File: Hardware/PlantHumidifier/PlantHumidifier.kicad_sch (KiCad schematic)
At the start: 12 parts

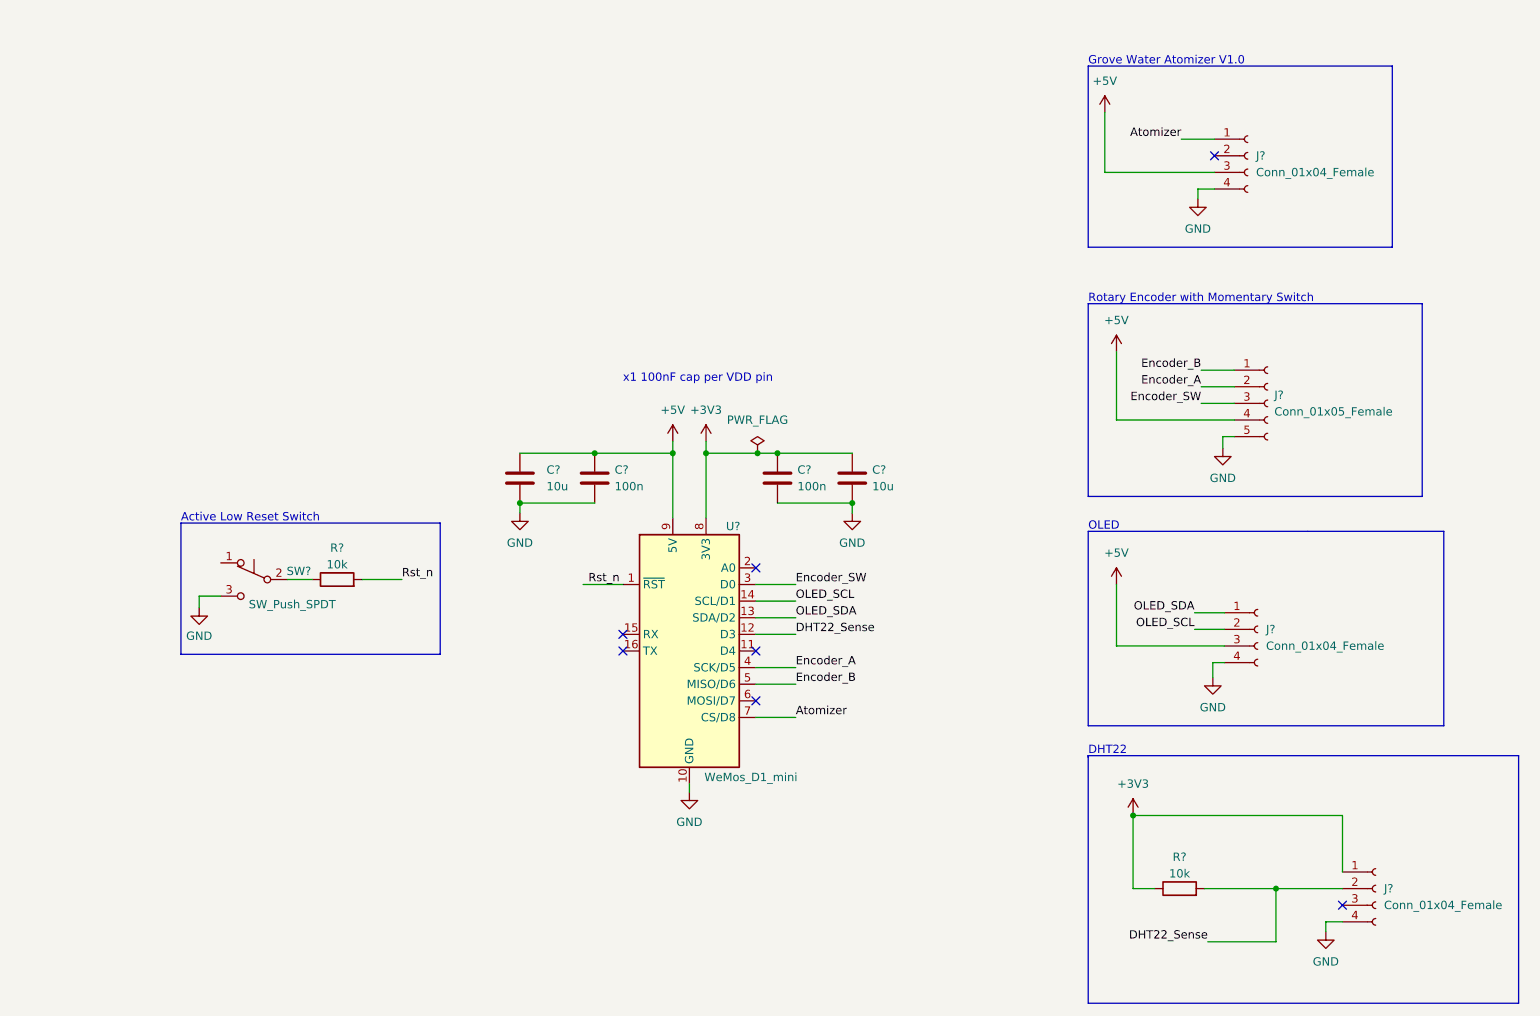
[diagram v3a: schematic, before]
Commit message: Schematic: Finish adding title and drawing outlines for different modules
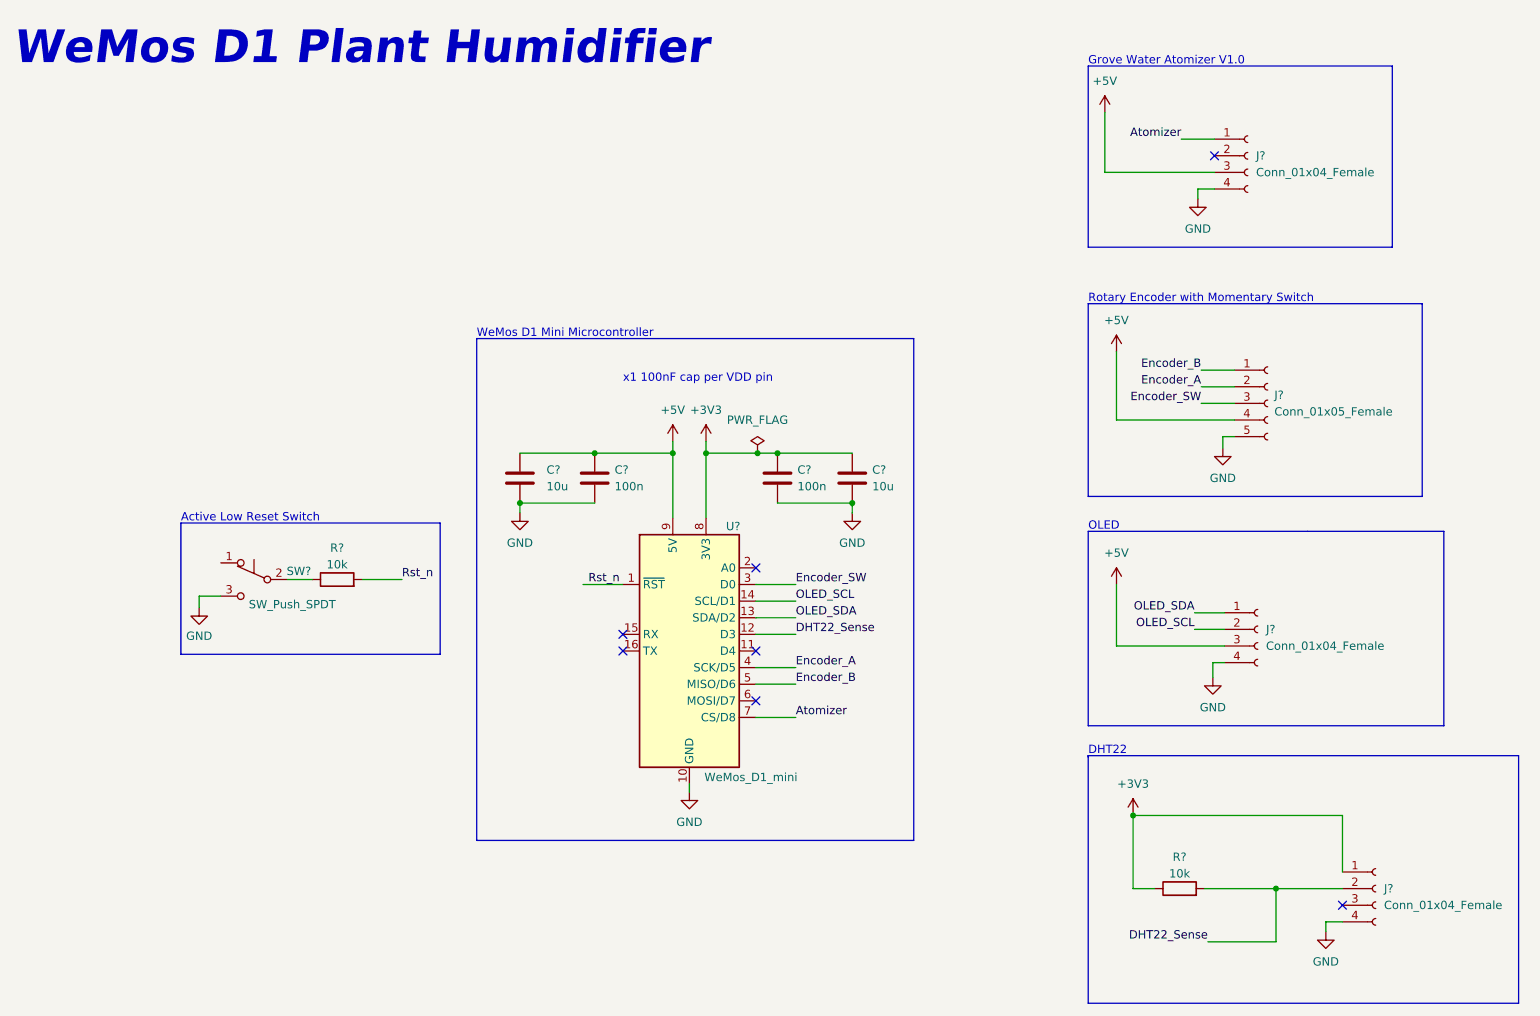
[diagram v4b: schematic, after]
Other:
- note added: "WeMos D1 Mini Microcontroller"
- note added: "WeMos D1 Plant Humidifier"
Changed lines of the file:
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@@
+    (stroke (width 0) (type default) (color 0 0 0 0))
+  )
+  (polyline (pts (xy 149.606 60.706) (xy 149.606 137.414))
     (stroke (width 0) (type default) (color 0 0 0 0))
   )
@@
     (stroke (width 0) (type default) (color 0 0 0 0))
   )
+  (polyline (pts (xy 82.804 137.414) (xy 82.804 60.706))
+    (stroke (width 0) (type default) (color 0 0 0 0))
+  )
   (wire (pts (xy 117.856 76.454) (xy 117.856 78.232))
     (stroke (width 0) (type default) (color 0 0 0 0))
@@
     (stroke (width 0) (type default) (color 0 0 0 0))
   )
+  (polyline (pts (xy 149.606 137.414) (xy 82.804 137.414))
+    (stroke (width 0) (type default) (color 0 0 0 0))
+  )
   (wire (pts (xy 178.816 26.162) (xy 178.816 35.306))
     (stroke (width 0) (type default) (color 0 0 0 0))
@@
     (stroke (width 0) (type default) (color 0 0 0 0))
   )
+  (polyline (pts (xy 82.804 60.706) (xy 149.606 60.706))
+    (stroke (width 0) (type default) (color 0 0 0 0))
+  )
   (polyline (pts (xy 37.592 108.966) (xy 37.592 88.9))
     (stroke (width 0) (type default) (color 0 0 0 0))
@@
     (effects (font (size 1.27 1.27)) (justify left bottom))
   )
+  (text "WeMos D1 Mini Microcontroller" (at 82.804 60.706 0)
+    (effects (font (size 1.27 1.27)) (justify left bottom))
+  )
   (text "Active Low Reset Switch" (at 37.592 88.9 0)
     (effects (font (size 1.27 1.27)) (justify left bottom))
   )
+  (text "WeMos D1 Plant Humidifier" (at 11.938 19.304 0)
+    (effects (font (size 5 5) (thickness 0.508) bold italic) (justify left bottom))
+  )
   (label "OLED_SDA" (at 131.572 103.378 0)

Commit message: Schematic: Annotate schematic
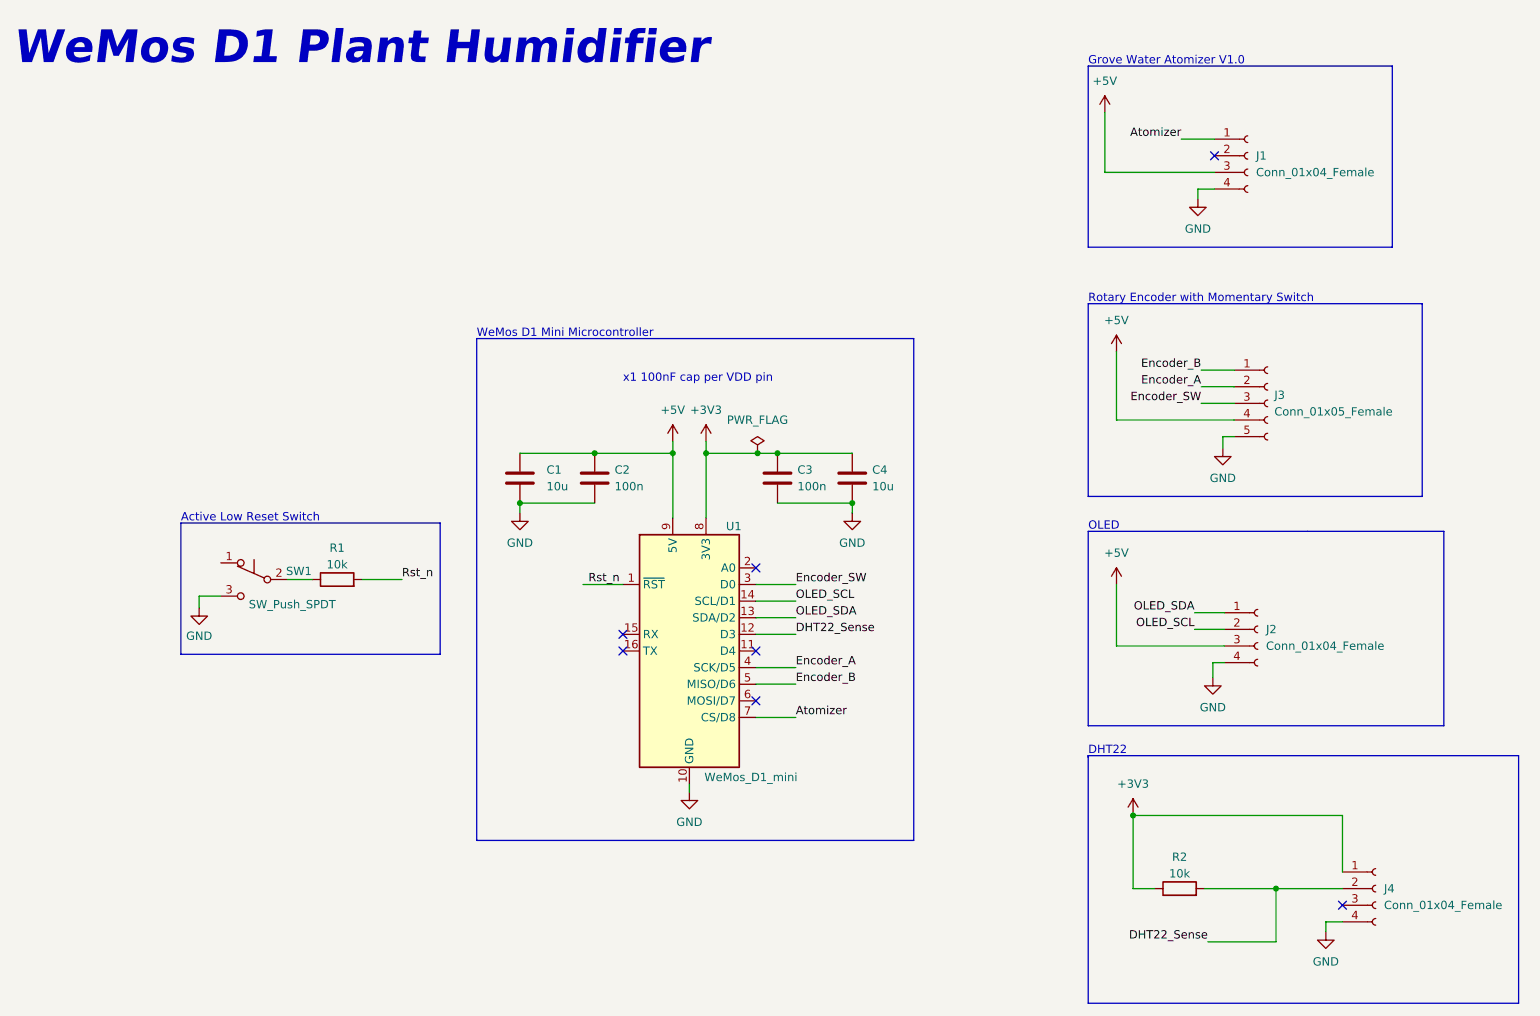
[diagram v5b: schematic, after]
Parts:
- gave numbers to parts that had none: 12

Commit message: Schematic: Run and fix DRC + Add power
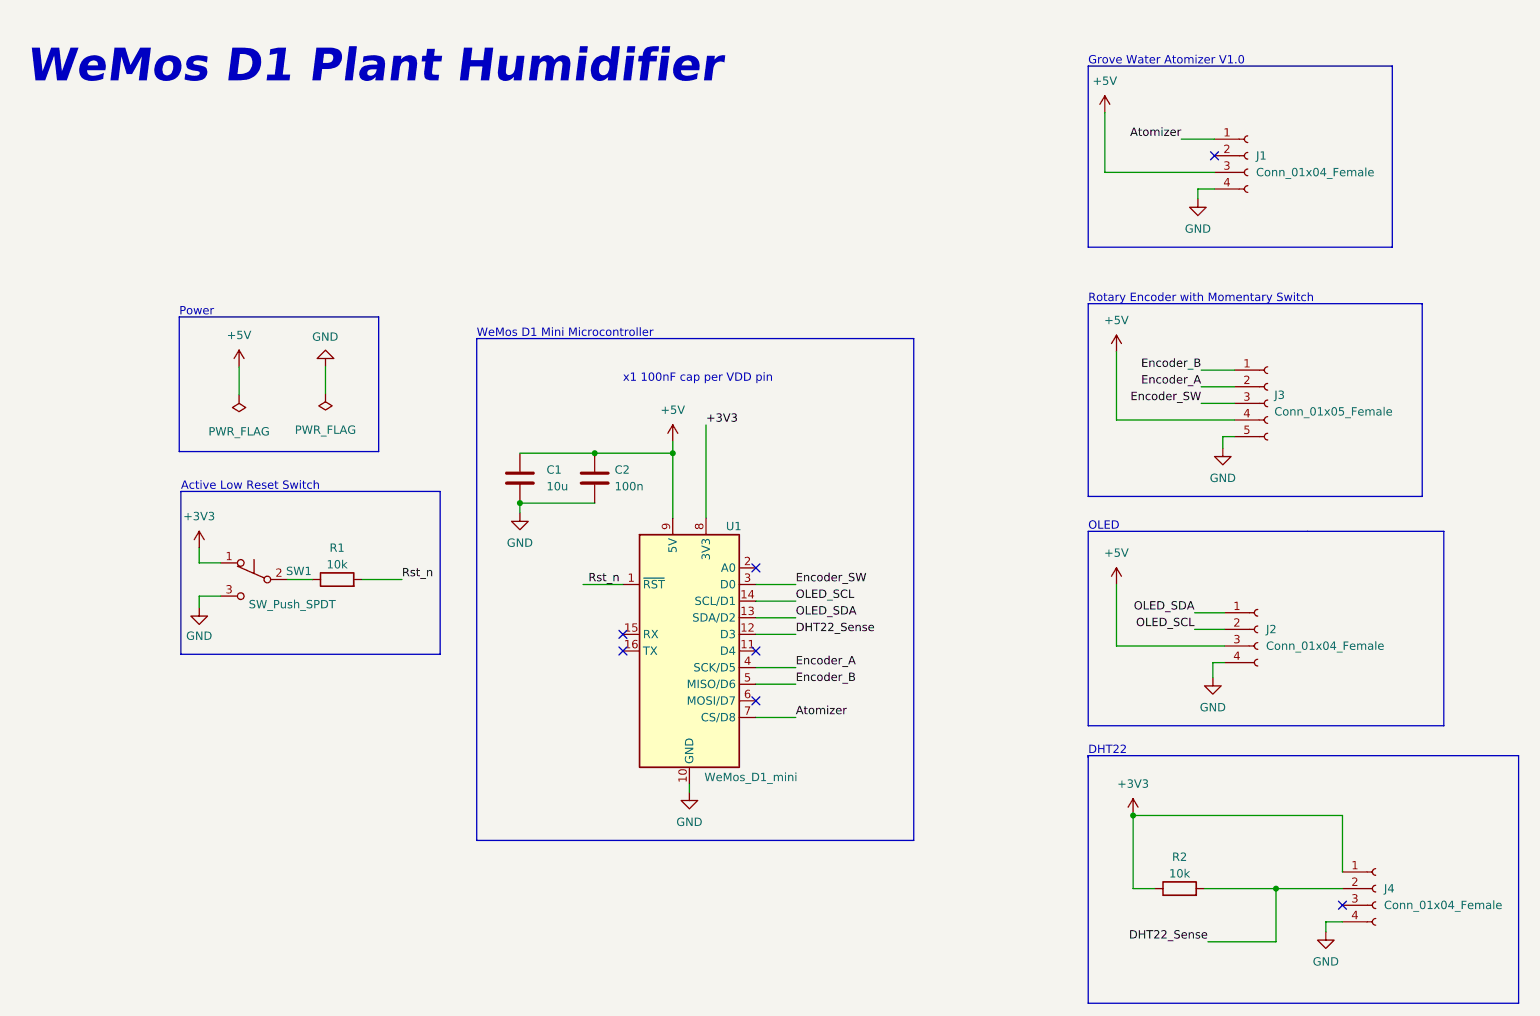
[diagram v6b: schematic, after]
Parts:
- removed C3: 100n, symbol Device:C
- removed C4: 10u, symbol Device:C
- C1: footprint (none) -> Capacitor_SMD:C_0603_1608Metric
- C2: footprint (none) -> Capacitor_SMD:C_0402_1005Metric
- J1: footprint (none) -> Connector_JST:JST_EH_B4B-EH-A_1x04_P2.50mm_Vertical
- J2, J4: footprint (none) -> Connector_JST:JST_XH_B4B-XH-A_1x04_P2.50mm_Vertical
- J3: footprint (none) -> Connector_JST:JST_XH_S5B-XH-A_1x05_P2.50mm_Horizontal
- R1, R2: footprint (none) -> Resistor_SMD:R_0402_1005Metric
- SW1: footprint (none) -> Button_Switch_SMD:SW_SPDT_PCM12
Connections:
- net +3V3: now also SW1.1 (A)
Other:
- note added: "Power"

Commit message: Schematic: Fix switch to momentary switch
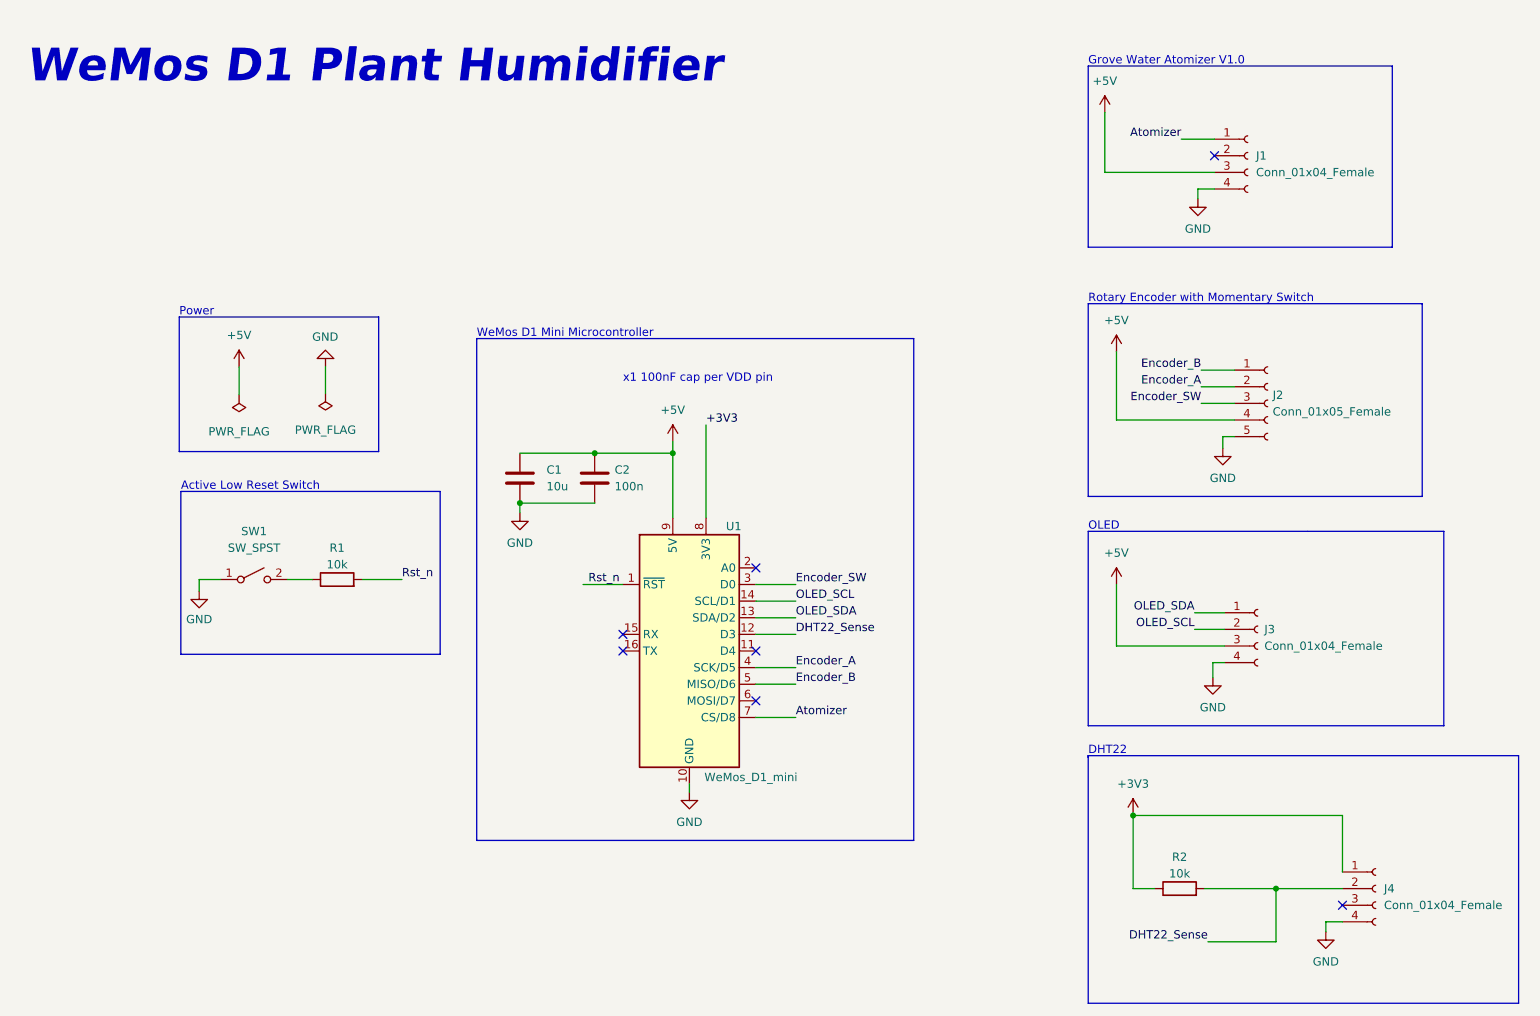
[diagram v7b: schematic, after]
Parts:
- removed SW1: SW_Push_SPDT, Button_Switch_SMD:SW_SPDT_PCM12, symbol Switch:SW_Push_SPDT
- added SW1: SW_SPST, symbol Switch:SW_SPST
- renumbered J3 to J2, J2 to J3
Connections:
- net GND: now also SW1.1 (A)
- net at R1.1: now also SW1.2 (B)

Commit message: Schematic: Add footprints (except for water atomizer)
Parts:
- J1: footprint Connector_JST:JST_EH_B4B-EH-A_1x04_P2.50mm_Vertical -> Connector_JST:JST_PH_B4B-PH-K_1x04_P2.00mm_Vertical
- J2: footprint Connector_JST:JST_XH_S5B-XH-A_1x05_P2.50mm_Horizontal -> Connector_JST:JST_XH_B5B-XH-A_1x05_P2.50mm_Vertical
- SW1: footprint (none) -> Button_Switch_THT:SW_Tactile_SPST_Angled_PTS645Vx83-2LFS
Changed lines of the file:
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@@
       (effects (font (size 1.27 1.27)) (justify left))
     )
-    (property "Footprint" "Connector_JST:JST_EH_B4B-EH-A_1x04_P2.50mm_Vertical" (id 2) (at 200.66 32.766 0)
+    (property "Footprint" "Connector_JST:JST_PH_B4B-PH-K_1x04_P2.00mm_Vertical" (id 2) (at 200.66 32.766 0)
       (effects (font (size 1.27 1.27)) hide)
     )
@@
     (property "Reference" "SW1" (id 0) (at 48.768 90.17 0))
     (property "Value" "SW_SPST" (id 1) (at 48.768 92.71 0))
-    (property "Footprint" "" (id 2) (at 48.768 97.536 0)
+    (property "Footprint" "Button_Switch_THT:SW_Tactile_SPST_Angled_PTS645Vx83-2LFS" (id 2) (at 48.768 97.536 0)
       (effects (font (size 1.27 1.27)) hide)
     )
@@
       (effects (font (size 1.27 1.27)) (justify left))
     )
-    (property "Footprint" "Connector_JST:JST_XH_S5B-XH-A_1x05_P2.50mm_Horizontal" (id 2) (at 203.708 70.612 0)
+    (property "Footprint" "Connector_JST:JST_XH_B5B-XH-A_1x05_P2.50mm_Vertical" (id 2) (at 203.708 70.612 0)
       (effects (font (size 1.27 1.27)) hide)
     )
@@
     )
     (path "/2394e559-b98a-40f6-b850-791be34e4734"
-      (reference "J1") (unit 1) (value "Conn_01x04_Female") (footprint "Connector_JST:JST_EH_B4B-EH-A_1x04_P2.50mm_Vertical")
+      (reference "J1") (unit 1) (value "Conn_01x04_Female") (footprint "Connector_JST:JST_PH_B4B-PH-K_1x04_P2.00mm_Vertical")
     )
     (path "/b462574f-43c5-4a1a-9527-fc39d017b1e6"
-      (reference "J2") (unit 1) (value "Conn_01x05_Female") (footprint "Connector_JST:JST_XH_S5B-XH-A_1x05_P2.50mm_Horizontal")
+      (reference "J2") (unit 1) (value "Conn_01x05_Female") (footprint "Connector_JST:JST_XH_B5B-XH-A_1x05_P2.50mm_Vertical")
     )
     (path "/83845b8d-1c62-4450-bceb-8208d6b21664"
@@
     )
     (path "/31337aab-e920-4411-a51b-1ee0c06a79e6"
-      (reference "SW1") (unit 1) (value "SW_SPST") (footprint "")
+      (reference "SW1") (unit 1) (value "SW_SPST") (footprint "Button_Switch_THT:SW_Tactile_SPST_Angled_PTS645Vx83-2LFS")
     )
     (path "/fb8daade-f4cb-4b21-85db-6e6f772ccb5f"
